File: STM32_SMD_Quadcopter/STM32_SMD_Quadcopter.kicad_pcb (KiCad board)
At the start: 4 copper layers, 43.8 x 26 mm, 61 parts, among them J1 PWR, J2 USB_B_Micro, J3 Micro_SD_Card, J4 DEBUG, M1 Brushed_DC, M2 Brushed_DC, M3 Brushed_DC, M4 Brushed_DC, Q1 IRLML6244TR, Q2 IRLML6244TR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

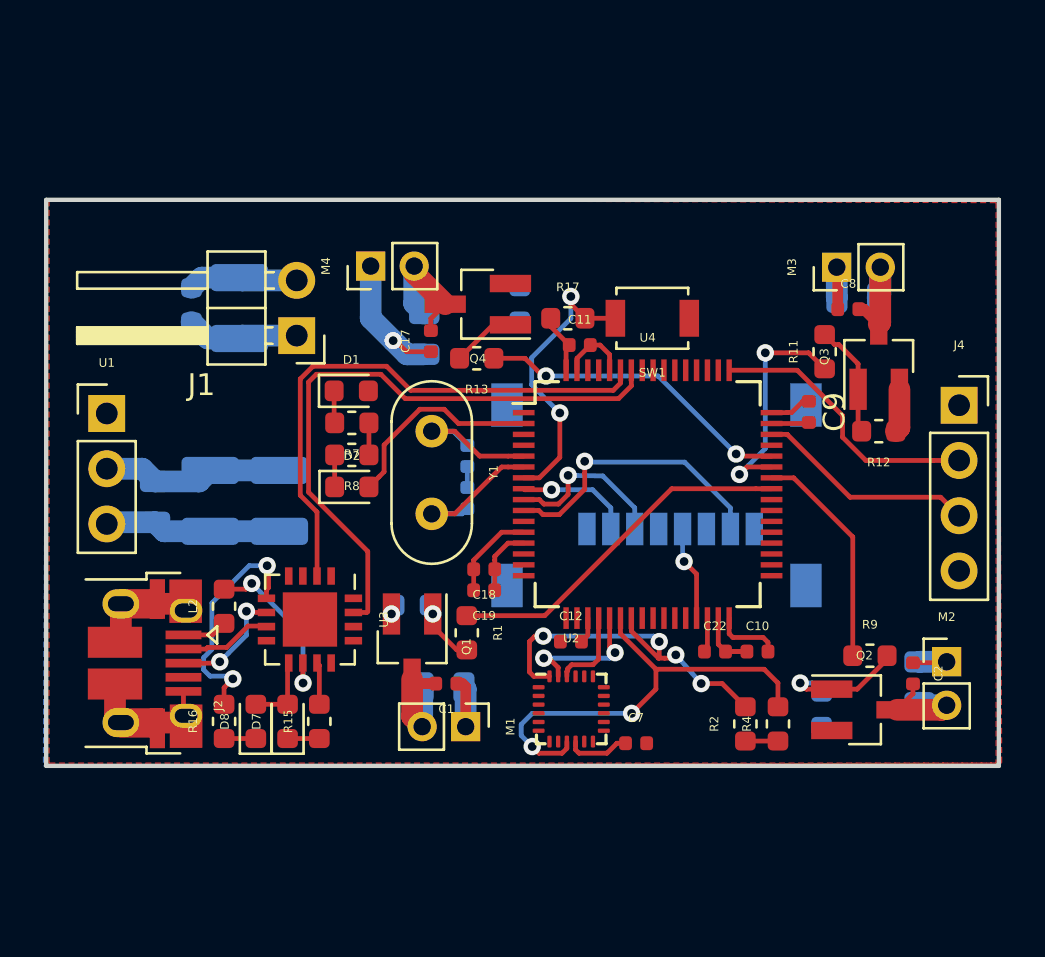
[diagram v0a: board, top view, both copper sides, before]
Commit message: regulator, power over USB, compact SMD, 0603 min cap size
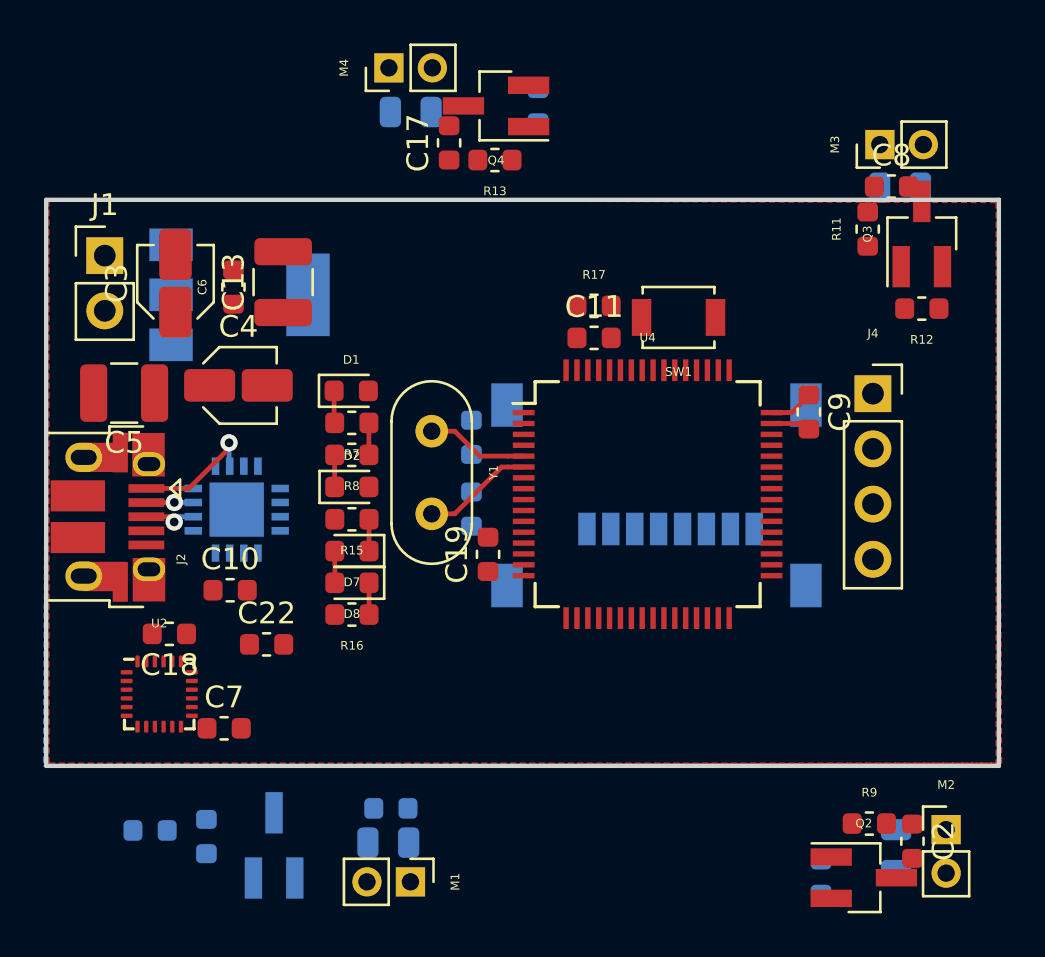
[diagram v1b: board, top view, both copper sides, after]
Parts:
- removed C12: 100nF, Capacitor_SMD:C_0402_1005Metric
- removed L2: 0.1uH, Inductor_SMD:L_0603_1608Metric
- removed R2, R4: 10K, Resistor_SMD:R_0603_1608Metric
- C1: footprint Capacitor_SMD:C_0402_1005Metric -> Capacitor_SMD:C_0603_1608Metric; moved to B.Cu
- C10, C11, C17, C18, C19, C2, C20, C21, C22, C7, C8, C9: footprint Capacitor_SMD:C_0402_1005Metric -> Capacitor_SMD:C_0603_1608Metric
- C13, C6: moved to F.Cu
- C3, C4: footprint Capacitor_SMD:C_1210_3225Metric -> Capacitor_SMD:C_Elec_3x5.4; moved to F.Cu
- C5: footprint Capacitor_SMD:C_0805_2012Metric -> Capacitor_SMD:C_1210_3225Metric; moved to F.Cu
- J1: footprint Connector_PinHeader_2.54mm:PinHeader_1x02_P2.54mm_Horizontal -> Connector_PinHeader_2.54mm:PinHeader_1x02_P2.54mm_Vertical
- Q1, R1, U3: moved to B.Cu
- U1: value LM1085-3.3 -> LT1129-3.3_SOT223; footprint Connector_PinHeader_2.54mm:PinHeader_1x03_P2.54mm_Vertical -> Package_TO_SOT_SMD:SOT-223-3_TabPin2; moved to B.Cu
- moved C10 24.4 mm to (102.4, 164.0)
- moved C22 20.6 mm to (104.1, 166.5)
- moved C7 19.0 mm to (102.2, 170.4)
- moved U2 19.0 mm to (99.2, 168.8)
- moved R3 15.9 mm to (98.8, 175.1)
- moved R1 15.2 mm to (101.3, 175.3), turned to 90 degrees
- moved C18 14.8 mm to (99.6, 166.0)
- moved Q1 11.1 mm to (104.5, 175.7), turned to 90 degrees
- moved D6 10.2 mm to (110.7, 142.0), turned to 0 degrees
- moved C13 10.1 mm to (104.9, 149.8)
- moved J1 9.57 mm to (96.7, 148.6), turned to 0 degrees
- moved R15 9.42 mm to (108.0, 160.7), turned to 180 degrees
- moved C17 9.16 mm to (112.5, 143.4)
- moved M4 9.16 mm to (109.7, 140.0)
- moved Q4 9.16 mm to (114.7, 141.7)
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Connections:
- C13 pad 1: +3V3 -> +BATT
- J2 pad 1: USB_VBUS -> VUSB
- J2 pad 4: (no net) -> Net-(J2-Pad4)
- J3 pad 1: (no net) -> Net-(J3-Pad1)
- J3 pad 8: (no net) -> Net-(J3-Pad8)
- U2 pad 11: (no net) -> Net-(U2-Pad11)
- U2 pad 12: (no net) -> Net-(U2-Pad12)
- U2 pad 21: (no net) -> Net-(U2-Pad21)
- U2 pad 7: (no net) -> Net-(U2-Pad7)
- U3 pad 10: Net-(L2-Pad2) -> VUSB
- U3 pad 12: (no net) -> Net-(U3-Pad12)
- U3 pad 14: (no net) -> Net-(U3-Pad14)
- U3 pad 16: (no net) -> Net-(U3-Pad16)
- U3 pad 4: (no net) -> Net-(U3-Pad4)
- U3 pad 8: (no net) -> +3V3
- U4 pad 11: (no net) -> Net-(U4-Pad11)
- U4 pad 14: (no net) -> Net-(U4-Pad14)
- U4 pad 15: (no net) -> Net-(U4-Pad15)
- U4 pad 16: (no net) -> Net-(U4-Pad16)
- U4 pad 17: (no net) -> Net-(U4-Pad17)
- U4 pad 24: (no net) -> Net-(U4-Pad24)
- U4 pad 25: (no net) -> Net-(U4-Pad25)
- U4 pad 26: (no net) -> Net-(U4-Pad26)
- U4 pad 27: (no net) -> Net-(U4-Pad27)
- U4 pad 28: (no net) -> Net-(U4-Pad28)
- U4 pad 3: (no net) -> Net-(U4-Pad3)
- U4 pad 33: (no net) -> Net-(U4-Pad33)
- U4 pad 34: (no net) -> Net-(U4-Pad34)
- U4 pad 35: (no net) -> Net-(U4-Pad35)
- U4 pad 36: (no net) -> Net-(U4-Pad36)
- U4 pad 37: (no net) -> Net-(U4-Pad37)
- U4 pad 38: (no net) -> Net-(U4-Pad38)
- U4 pad 39: (no net) -> Net-(U4-Pad39)
- U4 pad 4: (no net) -> Net-(U4-Pad4)
- U4 pad 40: (no net) -> Net-(U4-Pad40)
- U4 pad 45: (no net) -> Net-(U4-Pad45)
- U4 pad 50: (no net) -> Net-(U4-Pad50)
- U4 pad 51: (no net) -> Net-(U4-Pad51)
- U4 pad 52: (no net) -> Net-(U4-Pad52)
- U4 pad 53: (no net) -> Net-(U4-Pad53)
- U4 pad 54: (no net) -> Net-(U4-Pad54)
- U4 pad 55: (no net) -> Net-(U4-Pad55)
- U4 pad 56: (no net) -> Net-(U4-Pad56)
- U4 pad 57: (no net) -> Net-(U4-Pad57)
- U4 pad 61: (no net) -> Net-(U4-Pad61)
- U4 pad 62: (no net) -> Net-(U4-Pad62)
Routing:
- net GND: track 42.5 -> 3.14 mm, vias 1 -> 0
- net USART1_TX: track 28.8 -> 0.00 mm
- net USART1_RX: track 25.5 -> 0.00 mm
- net +BATT: track 22.9 -> 0.00 mm, vias 1 -> 0
- net +3V3: track 25.2 -> 3.11 mm
- net SPI1_MISO: track 21.1 -> 0.00 mm, vias 2 -> 0
- net SPI1_MOSI: track 17.0 -> 0.00 mm, vias 4 -> 0
- net MOTOR_A: track 16.4 -> 0.00 mm
- net MOTOR_D: track 14.6 -> 0.00 mm, vias 2 -> 0
- net Net-(R17-Pad2): track 13.5 -> 0.00 mm, vias 2 -> 0
- net SPI2_MISO: track 13.2 -> 0.00 mm, vias 1 -> 0
- net SYS_JTCL-SWCLK: track 12.9 -> 0.00 mm
- net Net-(R16-Pad2): track 11.0 -> 0.00 mm, vias 2 -> 0
- net MOTOR_C: track 10.8 -> 0.00 mm, vias 2 -> 0
- net MOTOR_B: track 10.3 -> 0.00 mm
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- removed copper zone on In2.Cu, net +BATT
- removed copper zone on In1.Cu, net GND
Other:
- copper layers 4 -> 2

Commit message: Latest model, no traces, old crystal
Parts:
- C1, C20, C21, Q1, R1: moved to F.Cu
- C19, C5, R12: moved to B.Cu
- J2: footprint Connector_USB:USB_Micro-B_Amphenol_10103594-0001LF_Horizontal -> Connector_USB:USB_Micro-B_Molex_47346-0001
- J3: footprint Connector_Card:microSD_HC_Wuerth_693072010801 -> Connector_Card:microSD_HC_Hirose_DM3D-SF
- Y1: footprint Crystal:Crystal_HC52-U_Vertical -> Crystal:Crystal_SMD_HC49-SD
- moved C19 142.5 mm to (67.2, 27.9), turned to 180 degrees
- moved R10 139.1 mm to (79.5, 47.5), turned to 0 degrees
- moved Q2 138.3 mm to (79.5, 49.1), turned to 270 degrees
- moved D3 137.9 mm to (58.7, 47.5)
- moved M1 137.6 mm to (59.8, 49.6)
- moved D4 137.0 mm to (83.8, 48.1), turned to 180 degrees
- moved R9 136.8 mm to (82.0, 47.3), turned to 270 degrees
- moved C2 136.8 mm to (84.2, 48.1), turned to 180 degrees
- moved Q1 136.7 mm to (54.5, 48.4), turned to 270 degrees
- moved C1 136.4 mm to (59.2, 47.4)
- moved R1 136.1 mm to (57.0, 46.7), turned to 270 degrees
- moved R3 135.6 mm to (54.6, 46.9)
- moved M2 134.6 mm to (84.7, 50.3), turned to 270 degrees
- moved C5 134.2 mm to (53.4, 28.3)
- moved U2 132.8 mm to (46.2, 47.0)
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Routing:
- net GND: track 3.14 -> 11.4 mm
- net +BATT: track 0.00 -> 8.24 mm
- net VUSB: track 5.91 -> 0.00 mm, vias 1 -> 0
- net Net-(C21-Pad2): track 5.12 -> 0.00 mm
- net Net-(C20-Pad2): track 4.71 -> 0.00 mm
- net Net-(J2-Pad3): track 2.43 -> 0.00 mm, vias 1 -> 0
- net Net-(J2-Pad2): track 2.16 -> 0.00 mm, vias 1 -> 0
- net +3V3: track 3.11 -> 4.63 mm
- net Net-(D1-Pad1): track 1.48 -> 0.00 mm
- net Net-(D2-Pad1): track 1.47 -> 0.00 mm
- net Net-(C17-Pad2): track 0.56 -> 0.00 mm
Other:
- net class Power3 added: clearance 0.1, trace_width 1.5, via_dia 0.8, via_drill 0.4

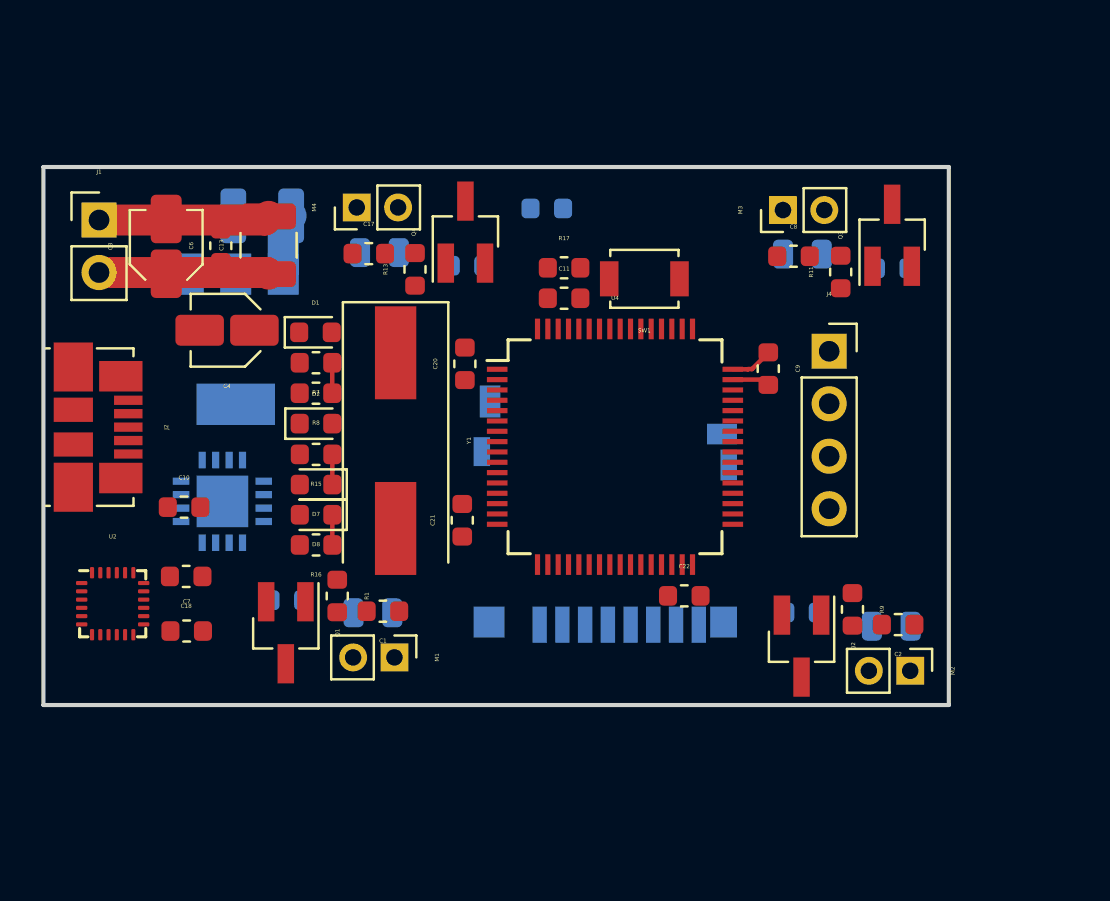
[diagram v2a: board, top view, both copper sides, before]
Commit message: Made much denser, added traces
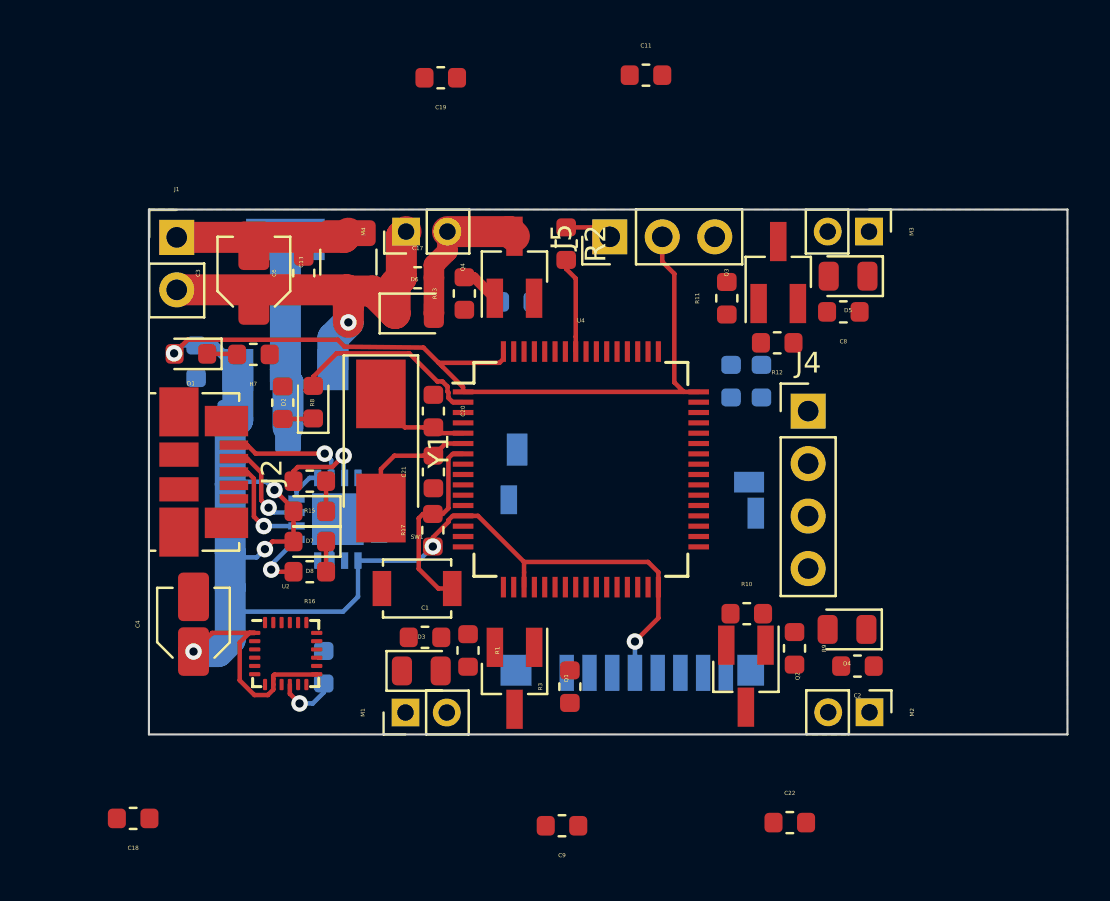
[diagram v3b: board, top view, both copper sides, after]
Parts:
- added J5: DSMX, Connector_PinHeader_2.54mm:PinHeader_1x03_P2.54mm_Vertical, F.Cu at (70.2, 29.3)
- added R2: 220, Resistor_SMD:R_0603_1608Metric, F.Cu at (68.1, 29.6)
- added R4: 3K, Resistor_SMD:R_0603_1608Metric, B.Cu at (77.5, 36.3)
- added R5: 10K, Resistor_SMD:R_0603_1608Metric, B.Cu at (76.1, 36.3)
- C10, C7: moved to B.Cu
- C19, D3, D4, D5, D6, R10, R12, R3: moved to F.Cu
- J4: footprint Connector_PinSocket_2.54mm:PinSocket_1x04_P2.54mm_Vertical -> Connector_PinHeader_2.54mm:PinHeader_1x04_P2.54mm_Vertical
- R7, R8: value R -> 470
- Y1: value 8MHz -> 8MHz ECS801830JGNTR; footprint Crystal:Crystal_SMD_HC49-SD -> Crystal:Crystal_SMD_Abracon_ABM3-2Pin_5.0x3.2mm_HandSoldering
- moved C9 24.3 mm to (67.9, 57.8), turned to 180 degrees
- moved SW1 18.6 mm to (60.9, 46.3), turned to 0 degrees
- moved R3 14.3 mm to (68.3, 51.1), turned to 90 degrees
- moved C4 14.3 mm to (50.1, 48.0), turned to 90 degrees
- moved R17 14.2 mm to (61.6, 43.5), turned to 90 degrees
- moved C22 12.1 mm to (78.9, 57.6)
- moved C18 12.0 mm to (47.1, 57.4)
- moved C11 11.5 mm to (72.0, 21.5)
- moved Q1 11.3 mm to (65.6, 50.6)
- moved C5 10.2 mm to (53.2, 38.5), turned to 0 degrees
- moved U2 8.71 mm to (54.5, 49.5)
- moved C19 8.14 mm to (62.0, 21.6)
- moved C10 7.06 mm to (50.2, 35.3), turned to 90 degrees
- moved C7 6.86 mm to (56.4, 50.1), turned to 90 degrees
- moved R1 6.86 mm to (63.3, 49.3)
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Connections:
- J2 pad 4: Net-(J2-Pad4) -> (no net)
- J3 pad 1: Net-(J3-Pad1) -> (no net)
- J3 pad 3: SPI2_MOSI -> SPI1_MOSI
- J3 pad 5: SPI2_SCK -> SPI1_SCK
- J3 pad 7: SPI2_MISO -> SPI1_MISO
- J3 pad 8: Net-(J3-Pad8) -> (no net)
- U2 pad 11: Net-(U2-Pad11) -> (no net)
- U2 pad 12: Net-(U2-Pad12) -> (no net)
- U2 pad 21: Net-(U2-Pad21) -> (no net)
- U2 pad 23: SPI1_SCK -> SPI2_SCK
- U2 pad 24: SPI1_MOSI -> SPI2_MOSI
- U2 pad 7: Net-(U2-Pad7) -> (no net)
- U2 pad 9: SPI1_MISO -> SPI2_MISO
- U3 pad 12: Net-(U3-Pad12) -> (no net)
- U3 pad 14: Net-(U3-Pad14) -> (no net)
- U3 pad 16: Net-(U3-Pad16) -> (no net)
- U3 pad 4: Net-(U3-Pad4) -> (no net)
- U4 pad 11: Net-(U4-Pad11) -> (no net)
- U4 pad 14: Net-(U4-Pad14) -> (no net)
- U4 pad 15: Net-(U4-Pad15) -> (no net)
- U4 pad 16: Net-(U4-Pad16) -> (no net)
- U4 pad 17: Net-(U4-Pad17) -> (no net)
- U4 pad 20: MPU9250_CS -> SD_CARD_CS
- U4 pad 24: Net-(U4-Pad24) -> (no net)
- U4 pad 25: Net-(U4-Pad25) -> (no net)
- U4 pad 26: Net-(U4-Pad26) -> (no net)
- U4 pad 27: Net-(U4-Pad27) -> (no net)
- U4 pad 28: Net-(U4-Pad28) -> (no net)
- U4 pad 3: Net-(U4-Pad3) -> (no net)
- U4 pad 33: Net-(U4-Pad33) -> (no net)
- U4 pad 34: Net-(U4-Pad34) -> (no net)
- U4 pad 35: Net-(U4-Pad35) -> (no net)
- U4 pad 36: Net-(U4-Pad36) -> (no net)
- U4 pad 37: Net-(U4-Pad37) -> (no net)
- U4 pad 38: Net-(U4-Pad38) -> (no net)
- U4 pad 39: Net-(U4-Pad39) -> (no net)
- U4 pad 4: Net-(U4-Pad4) -> (no net)
- U4 pad 40: Net-(U4-Pad40) -> (no net)
- U4 pad 45: Net-(U4-Pad45) -> VSENSE
- U4 pad 50: Net-(U4-Pad50) -> (no net)
- U4 pad 51: Net-(U4-Pad51) -> (no net)
- U4 pad 52: Net-(U4-Pad52) -> (no net)
- U4 pad 53: Net-(U4-Pad53) -> (no net)
- U4 pad 54: Net-(U4-Pad54) -> (no net)
- U4 pad 55: Net-(U4-Pad55) -> (no net)
- U4 pad 56: Net-(U4-Pad56) -> (no net)
- U4 pad 57: Net-(U4-Pad57) -> DSMX
- U4 pad 61: Net-(U4-Pad61) -> (no net)
- U4 pad 62: Net-(U4-Pad62) -> (no net)
- U4 pad 8: SD_CARD_CS -> MPU9250_CS
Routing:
- net +3V3: track 4.63 -> 111.0 mm, vias 0 -> 6
- net +BATT: track 8.24 -> 19.3 mm, vias 0 -> 1
- net GND: track 11.4 -> 22.1 mm
- net Status: track 0.00 -> 9.44 mm
- net Net-(R17-Pad2): track 0.00 -> 9.32 mm
- net Net-(C17-Pad2): track 0.00 -> 7.57 mm
- net Net-(C21-Pad2): track 0.00 -> 6.37 mm
- net VUSB: track 0.00 -> 5.87 mm, vias 0 -> 1
- net Net-(J2-Pad3): track 0.00 -> 5.19 mm, vias 0 -> 1
- net Net-(C20-Pad2): track 0.00 -> 5.04 mm
- net Net-(J2-Pad2): track 0.00 -> 4.90 mm, vias 0 -> 1
- net DSMX: track 0.00 -> 4.63 mm
- net Net-(R15-Pad2): track 0.00 -> 4.31 mm, vias 0 -> 1
- net Net-(R16-Pad2): track 0.00 -> 3.09 mm, vias 0 -> 1
- net Net-(C7-Pad1): track 0.00 -> 2.93 mm, vias 0 -> 1
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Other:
- board size 43.8 x 26 mm -> 44.4 x 25.4 mm

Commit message: Completed board v1
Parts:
- C10: moved to F.Cu
- J3: value Micro_SD_Card -> Micro_SD_Card_Det
- J4: footprint Connector_PinHeader_2.54mm:PinHeader_1x04_P2.54mm_Vertical -> STM32_SMD_Quadcopter:Harwin_M20-89004xx_1x04_P2.54mm_Horizontal_MODIFIEDSILKSCREEN
- moved C18 28.5 mm to (73.7, 47.2), turned to 90 degrees
- moved C9 18.4 mm to (50.5, 51.8), turned to 0 degrees
- moved C19 14.2 mm to (70.4, 33.0)
- moved C22 12.9 mm to (69.7, 48.7), turned to 180 degrees
- moved C11 11.8 mm to (73.5, 33.1)
- moved J4 4.64 mm to (83.5, 40.5)
- moved J3 2.14 mm to (70.0, 46.7)
- moved C10 1.50 mm to (49.8, 33.9), turned to 180 degrees
- moved D2 0.65 mm to (56.3, 37.8), turned to 270 degrees
- moved R8 0.62 mm to (54.7, 37.8)
- moved C4 0.61 mm to (50.7, 48.0)
- moved C2 0.54 mm to (81.7, 50.2)
- moved R7 0.43 mm to (52.8, 34.6)
- moved D1 0.36 mm to (49.8, 35.3)
- moved SW1 0.23 mm to (60.9, 46.1)
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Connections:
- J3 pad 10: (no net) -> GND
- J3 pad 11: (no net) -> GND
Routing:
- net +BATT: track 19.3 -> 112.4 mm, vias 1 -> 2
- net +3V3: track 111.0 -> 137.8 mm, vias 6 -> 8
- net MPU9250_CS: track 0.00 -> 24.3 mm, vias 0 -> 2
- net SPI2_MISO: track 0.00 -> 22.2 mm, vias 0 -> 2
- net SPI2_MOSI: track 0.00 -> 21.5 mm, vias 0 -> 2
- net SPI2_SCK: track 0.00 -> 19.2 mm
- net MOTOR_C: track 0.00 -> 18.9 mm
- net USART1_RX: track 0.00 -> 18.6 mm, vias 0 -> 3
- net MOTOR_A: track 0.00 -> 18.5 mm, vias 0 -> 2
- net SPI1_SCK: track 0.00 -> 18.5 mm, vias 0 -> 1
- net SPI1_MISO: track 0.00 -> 17.2 mm, vias 0 -> 1
- net MOTOR_D: track 0.00 -> 14.4 mm, vias 0 -> 2
- net USART1_TX: track 0.00 -> 14.0 mm, vias 0 -> 1
- net SYS_JTCL-SWCLK: track 0.00 -> 11.5 mm, vias 0 -> 2
- net MOTOR_B: track 0.00 -> 10.8 mm
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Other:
- board size 44.4 x 25.4 mm -> 36.5 x 25.4 mm
